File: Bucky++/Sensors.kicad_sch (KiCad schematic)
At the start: 25 parts, among them IC1 INA239AQDGSRQ1, IC2 INA239AQDGSRQ1, IC2001 INA239AQDGSRQ1, IC3 INA239AQDGSRQ1, IC6 INA239AQDGSRQ1

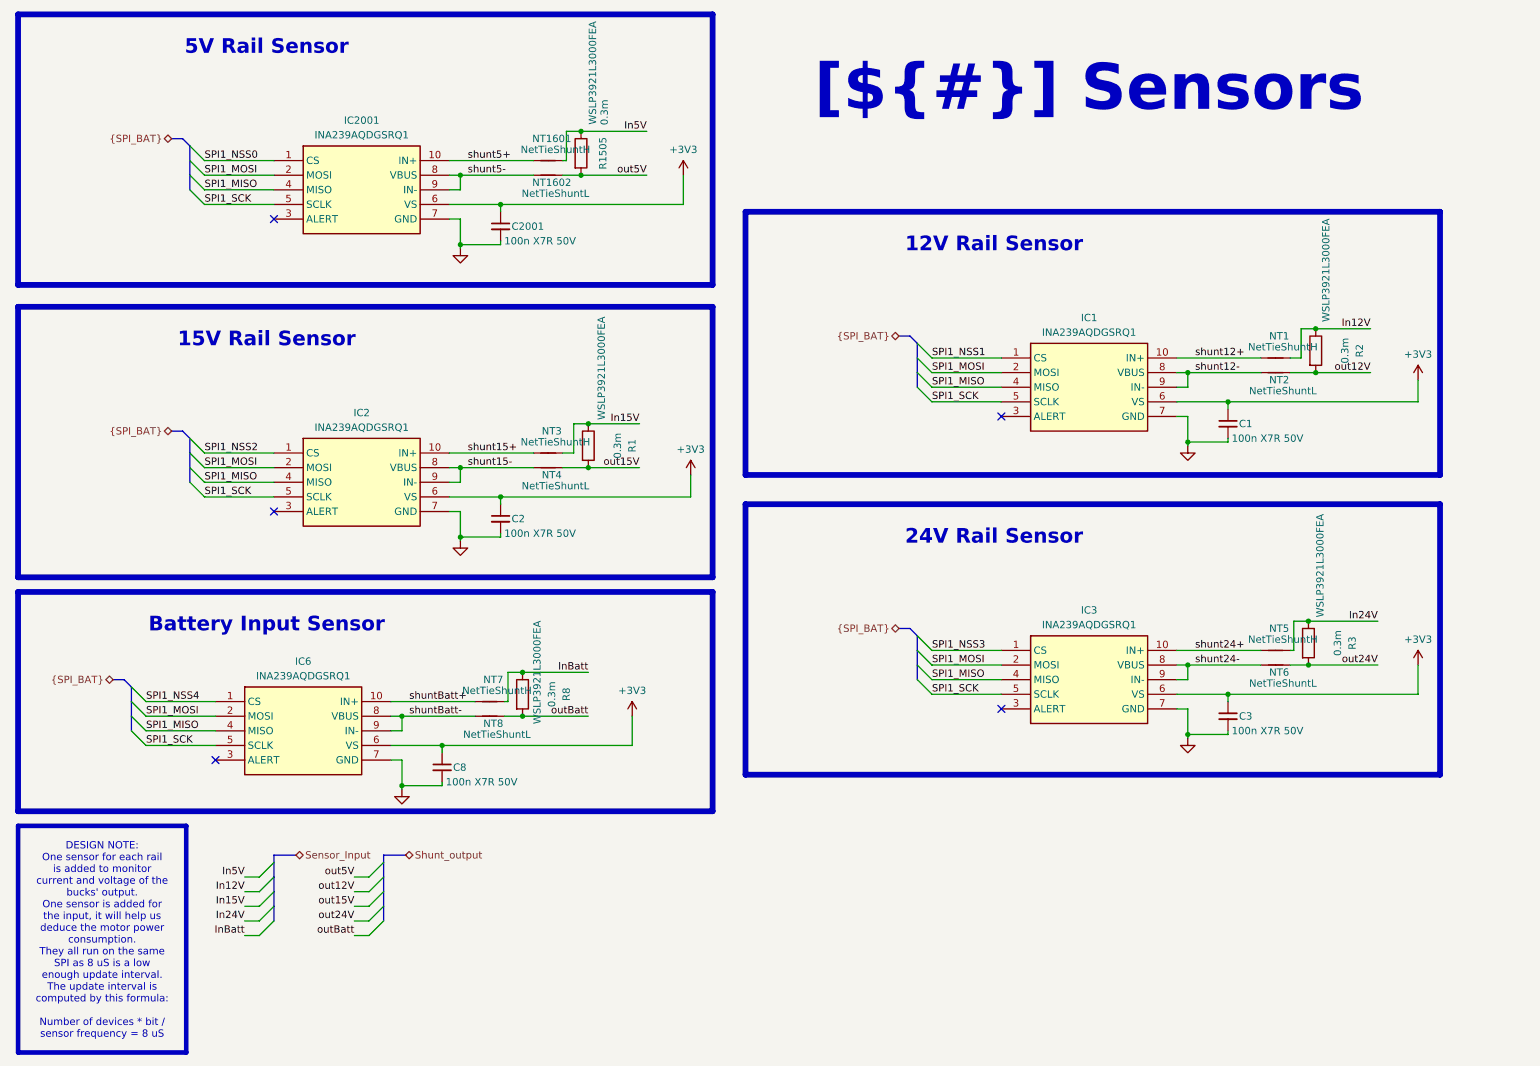
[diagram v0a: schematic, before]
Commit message: fixed errors and added protection diodes
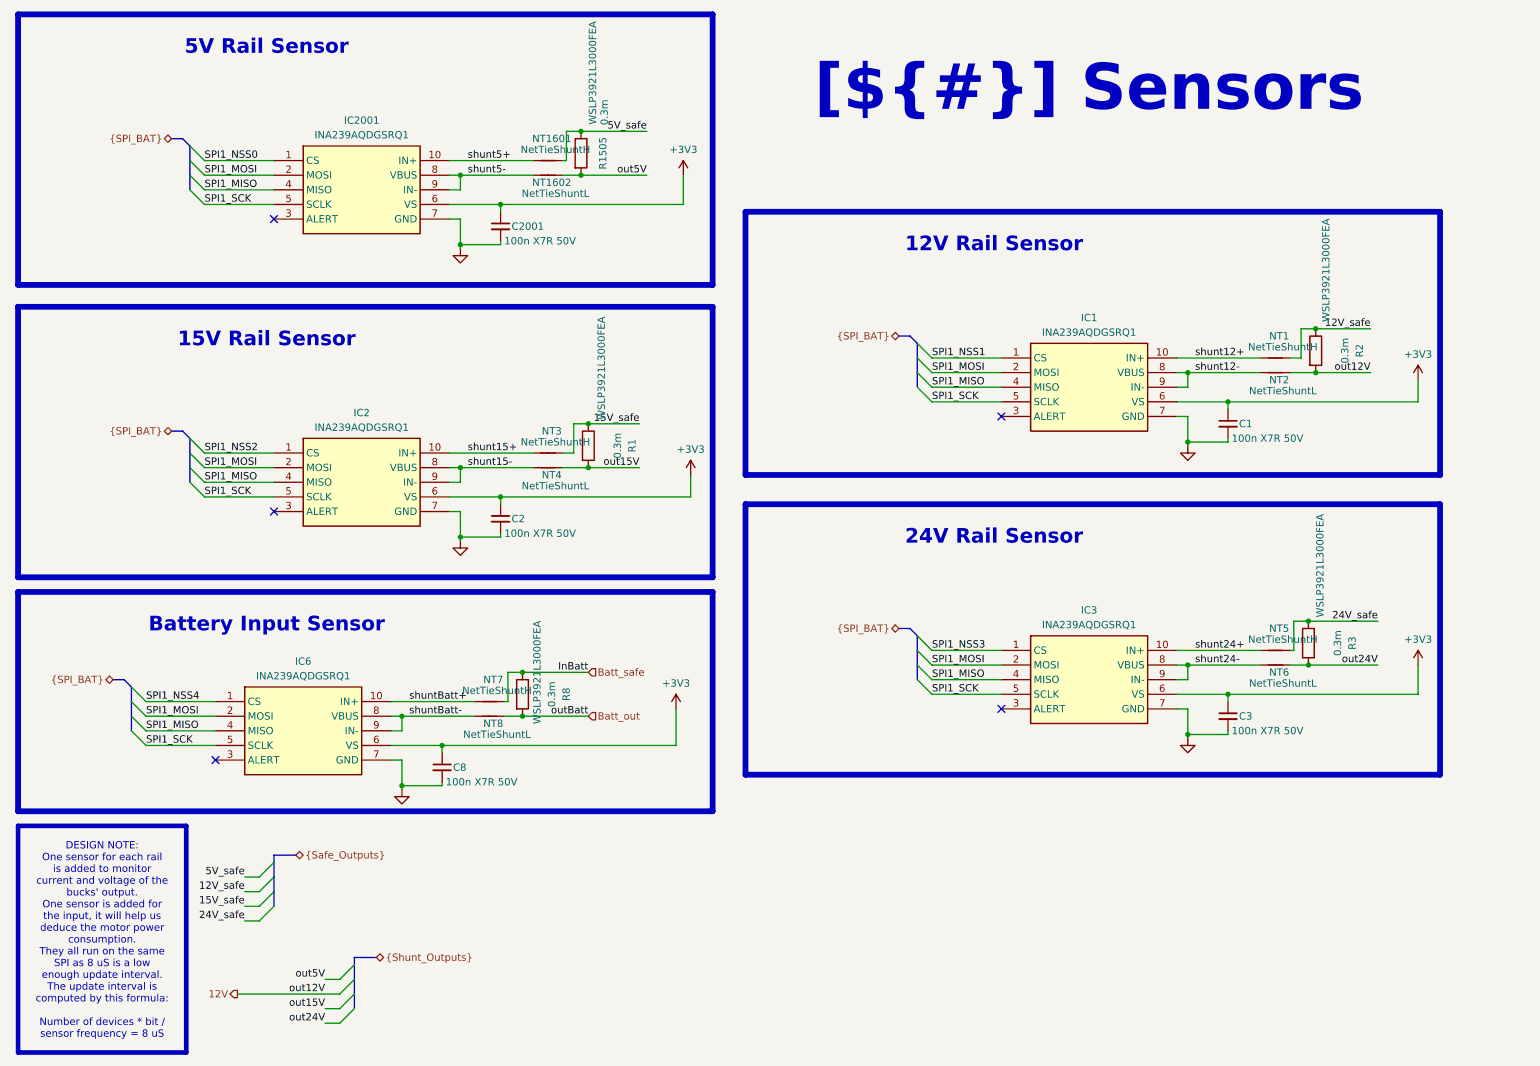
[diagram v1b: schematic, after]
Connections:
- net In12V renamed 12V_safe
- net In15V renamed 15V_safe
- net In24V renamed 24V_safe
- net In5V renamed 5V_safe
- net InBatt renamed Batt_safe
- net out12V renamed 12V
- net outBatt renamed Batt_out
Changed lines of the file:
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@@
 	)
 	(bus_entry
-		(at 77.47 167.64)
-		(size 2.54 -2.54)
-		(stroke
-			(width 0)
-			(type default)
-		)
-	)
-	(bus_entry
-		(at 77.47 175.26)
+		(at 72.39 185.42)
 		(size 2.54 -2.54)
 		(stroke
@@
 	)
 	(bus_entry
-		(at 58.42 175.26)
-		(size 2.54 -2.54)
-		(stroke
-			(width 0)
-			(type default)
-		)
-	)
-	(bus_entry
-		(at 77.47 170.18)
+		(at 72.39 187.96)
 		(size 2.54 -2.54)
 		(stroke
@@
 	)
 	(bus_entry
-		(at 77.47 165.1)
+		(at 72.39 182.88)
 		(size 2.54 -2.54)
 		(stroke
@@
 	)
 	(bus_entry
-		(at 77.47 172.72)
+		(at 72.39 190.5)
 		(size 2.54 -2.54)
 		(stroke
@@
 		)
 	)
-	(wire
-		(pts
-			(xy 74.93 167.64) (xy 77.47 167.64)
-		)
-		(stroke
-			(width 0)
-			(type default)
-		)
-	)
 	(bus
 		(pts
@@
 	(wire
 		(pts
-			(xy 55.88 175.26) (xy 58.42 175.26)
-		)
-		(stroke
-			(width 0)
-			(type default)
-		)
-	)
-	(wire
-		(pts
 			(xy 175.26 130.81) (xy 187.325 130.81)
 		)
@@
 	(wire
 		(pts
-			(xy 74.93 172.72) (xy 77.47 172.72)
+			(xy 69.85 190.5) (xy 72.39 190.5)
 		)
 		(stroke
@@
 	(wire
 		(pts
-			(xy 74.93 165.1) (xy 77.47 165.1)
+			(xy 54.61 185.42) (xy 72.39 185.42)
+		)
+		(stroke
+			(width 0)
+			(type default)
+		)
+	)
+	(wire
+		(pts
+			(xy 69.85 182.88) (xy 72.39 182.88)
 		)
 		(stroke
@@
 	(wire
 		(pts
-			(xy 123.19 137.16) (xy 123.19 142.24)
+			(xy 130.81 135.89) (xy 130.81 142.24)
 		)
 		(stroke
@@
 	(bus
 		(pts
-			(xy 80.01 170.18) (xy 80.01 167.64)
+			(xy 74.93 187.96) (xy 74.93 185.42)
 		)
 		(stroke
@@
 	(bus
 		(pts
-			(xy 80.01 162.56) (xy 80.01 161.29)
+			(xy 74.93 180.34) (xy 74.93 179.07)
 		)
 		(stroke
@@
 	(bus
 		(pts
-			(xy 60.96 170.18) (xy 60.96 172.72)
-		)
-		(stroke
-			(width 0)
-			(type default)
-		)
-	)
-	(bus
-		(pts
-			(xy 80.01 167.64) (xy 80.01 165.1)
+			(xy 74.93 185.42) (xy 74.93 182.88)
 		)
 		(stroke
@@
 		)
 	)
-	(wire
-		(pts
-			(xy 74.93 175.26) (xy 77.47 175.26)
-		)
-		(stroke
-			(width 0)
-			(type default)
-		)
-	)
 	(bus
 		(pts
@@
 		)
 	)
-	(bus
-		(pts
-			(xy 80.01 170.18) (xy 80.01 172.72)
-		)
-		(stroke
-			(width 0)
-			(type default)
-		)
-	)
 	(wire
 		(pts
@@
 	(wire
 		(pts
-			(xy 74.93 170.18) (xy 77.47 170.18)
+			(xy 69.85 187.96) (xy 72.39 187.96)
 		)
 		(stroke
@@
 	(bus
 		(pts
-			(xy 80.01 165.1) (xy 80.01 162.56)
+			(xy 74.93 182.88) (xy 74.93 180.34)
 		)
 		(stroke
@@
 	(wire
 		(pts
-			(xy 90.17 142.24) (xy 123.19 142.24)
+			(xy 90.17 142.24) (xy 130.81 142.24)
 		)
 		(stroke
@@
 	(bus
 		(pts
-			(xy 80.01 161.29) (xy 83.82 161.29)
+			(xy 74.93 179.07) (xy 78.74 179.07)
 		)
 		(stroke
@@
 	)
 	(label "out15V"
-		(at 74.93 170.18 180)
+		(at 69.85 187.96 180)
 		(effects
 			(font
@@
 		)
 	)
+	(label "24V_safe"
+		(at 252.73 120.65 180)
+		(effects
+			(font
+				(size 1.27 1.27)
+			)
+			(justify right bottom)
+		)
+	)
 	(label "SPI1_MOSI"
 		(at 48.895 43.18 0)
@@
 		)
 	)
-	(label "In15V"
-		(at 124.46 86.36 180)
-		(effects
-			(font
-				(size 1.27 1.27)
-			)
-			(justify right bottom)
-		)
-	)
-	(label "In15V"
+	(label "15V_safe"
 		(at 55.88 170.18 180)
 		(effects
@@
 		)
 	)
-	(label "In12V"
-		(at 251.46 69.85 180)
-		(effects
-			(font
-				(size 1.27 1.27)
-			)
-			(justify right bottom)
-		)
-	)
 	(label "SPI1_NSS3"
 		(at 175.26 125.73 0)
@@
 		)
 	)
-	(label "InBatt"
-		(at 55.88 175.26 180)
-		(effects
-			(font
-				(size 1.27 1.27)
-			)
-			(justify right bottom)
-		)
-	)
-	(label "In24V"
+	(label "24V_safe"
 		(at 55.88 172.72 180)
 		(effects
@@
 		)
 	)
-	(label "In12V"
+	(label "12V_safe"
 		(at 55.88 167.64 180)
 		(effects
@@
 	)
 	(label "out24V"
-		(at 74.93 172.72 180)
+		(at 69.85 190.5 180)
 		(effects
 			(font
@@
 		)
 	)
-	(label "In5V"
+	(label "5V_safe"
 		(at 55.88 165.1 180)
+		(effects
+			(font
+				(size 1.27 1.27)
+			)
+			(justify right bottom)
+		)
+	)
+	(label "5V_safe"
+		(at 125.73 35.56 180)
 		(effects
 			(font
@@
 		)
 	)
-	(label "In5V"
-		(at 125.73 35.56 180)
+	(label "15V_safe"
+		(at 124.46 86.36 180)
 		(effects
 			(font
@@
 		)
 	)
-	(label "In24V"
-		(at 252.73 120.65 180)
+	(label "12V_safe"
+		(at 251.46 69.85 180)
 		(effects
 			(font
@@
 		)
 	)
-	(label "outBatt"
-		(at 74.93 175.26 180)
-		(effects
-			(font
-				(size 1.27 1.27)
-			)
-			(justify right bottom)
-		)
-	)
 	(label "out12V"
-		(at 74.93 167.64 180)
+		(at 69.85 185.42 180)
 		(effects
 			(font
@@
 	)
 	(label "out5V"
-		(at 74.93 165.1 180)
+		(at 69.85 182.88 180)
 		(effects
 			(font
@@
 		)
 	)
-	(hierarchical_label "Sensor_Input"
+	(hierarchical_label "{Safe_Outputs}"
 		(shape tri_state)
 		(at 64.77 161.29 0)
@@
 		)
 	)
-	(hierarchical_label "Shunt_output"
+	(hierarchical_label "Batt_out"
+		(shape input)
+		(at 115.57 137.16 0)
+		(effects
+			(font
+				(size 1.27 1.27)
+			)
+			(justify left)
+		)
+	)
+	(hierarchical_label "12V"
+		(shape output)
+		(at 54.61 185.42 180)
+		(effects
+			(font
+				(size 1.27 1.27)
+			)
+			(justify right)
+		)
+	)
+	(hierarchical_label "{Shunt_Outputs}"
 		(shape tri_state)
-		(at 83.82 161.29 0)
+		(at 78.74 179.07 0)
+		(effects
+			(font
+				(size 1.27 1.27)
+			)
+			(justify left)
+		)
+	)
+	(hierarchical_label "Batt_safe"
+		(shape input)
+		(at 115.57 129.54 0)
 		(effects
 			(font
@@
 	(symbol
 		(lib_id "power:+3V3")
-		(at 123.19 137.16 0)
+		(at 130.81 135.89 0)
 		(unit 1)
 		(exclude_from_sim no)
@@
 		(fields_autoplaced yes)
 		(property "Reference" "#PWR017"
-			(at 123.19 140.97 0)
+			(at 130.81 139.7 0)
 			(effects
 				(font
@@
 		)
 		(property "Value" "+3V3"
-			(at 123.19 132.715 0)
+			(at 130.81 131.445 0)
 			(effects
 				(font
@@
 		)
 		(property "Footprint" ""
-			(at 123.19 137.16 0)
+			(at 130.81 135.89 0)
 			(effects
 				(font
@@
 		)
 		(property "Datasheet" ""
-			(at 123.19 137.16 0)
+			(at 130.81 135.89 0)
 			(effects
 				(font
@@
 		)
 		(property "Description" ""
-			(at 123.19 137.16 0)
-			(effects
-				(font
+			(at 130.81 135.89 0)
+			(effects
+				(font

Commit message: worked on layout, added adm1270
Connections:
- net 12V renamed out12V
- net 12V_safe renamed Vin_12V
- net 15V_safe renamed Vin_15V
- net 24V_safe renamed Vin_24V
- net 5V_safe renamed Vin_5V
- net Batt_out renamed Batt_protection
- net Batt_safe renamed Batt_in
